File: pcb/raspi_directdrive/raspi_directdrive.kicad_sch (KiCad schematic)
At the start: 9 parts, among them J1 Conn_01x02_Pin, J2 Conn_01x04_Pin, U1 L298HN, U2 L7805, U3 74LS86, U4 LM393

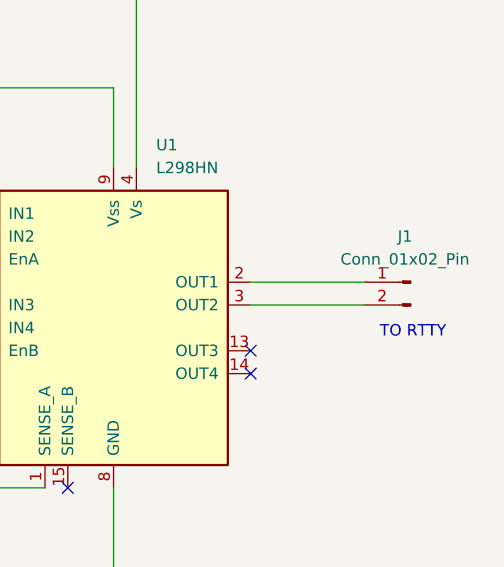
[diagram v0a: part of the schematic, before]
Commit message: change RTTY connection to use the appropriate audio jack instead of DuPont pins
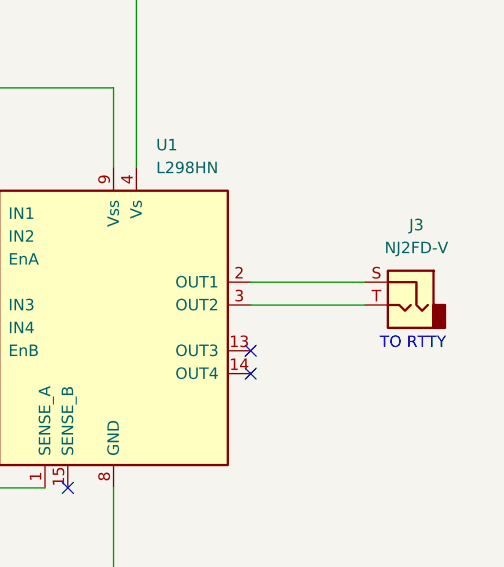
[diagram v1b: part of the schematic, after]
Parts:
- removed J1: Conn_01x02_Pin, symbol Connector:Conn_01x02_Pin
- added J3: NJ2FD-V, Connector_Audio:Jack_6.35mm_Neutrik_NJ2FD-V_Vertical, symbol Connector_Audio:NJ2FD-V
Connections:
- net at U1.2 (OUT1): now also J3.S
- net at U1.3 (OUT2): now also J3.T
